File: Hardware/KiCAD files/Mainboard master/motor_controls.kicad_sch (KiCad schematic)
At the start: 78 parts, among them J11 Conn_01x08, J12 Conn_01x08, J2 Conn_01x06, J4 Conn_01x06, J5 PINHD_1x8_Male, J6 Conn_01x06, J7 Conn_01x06, J9 PINHD_1x8_Male, U10 DRV8825PWPR, U4 DRV8825PWPR, U5 DRV8825PWPR, U8 DRV8825PWPR, U9 DRV8825PWPR

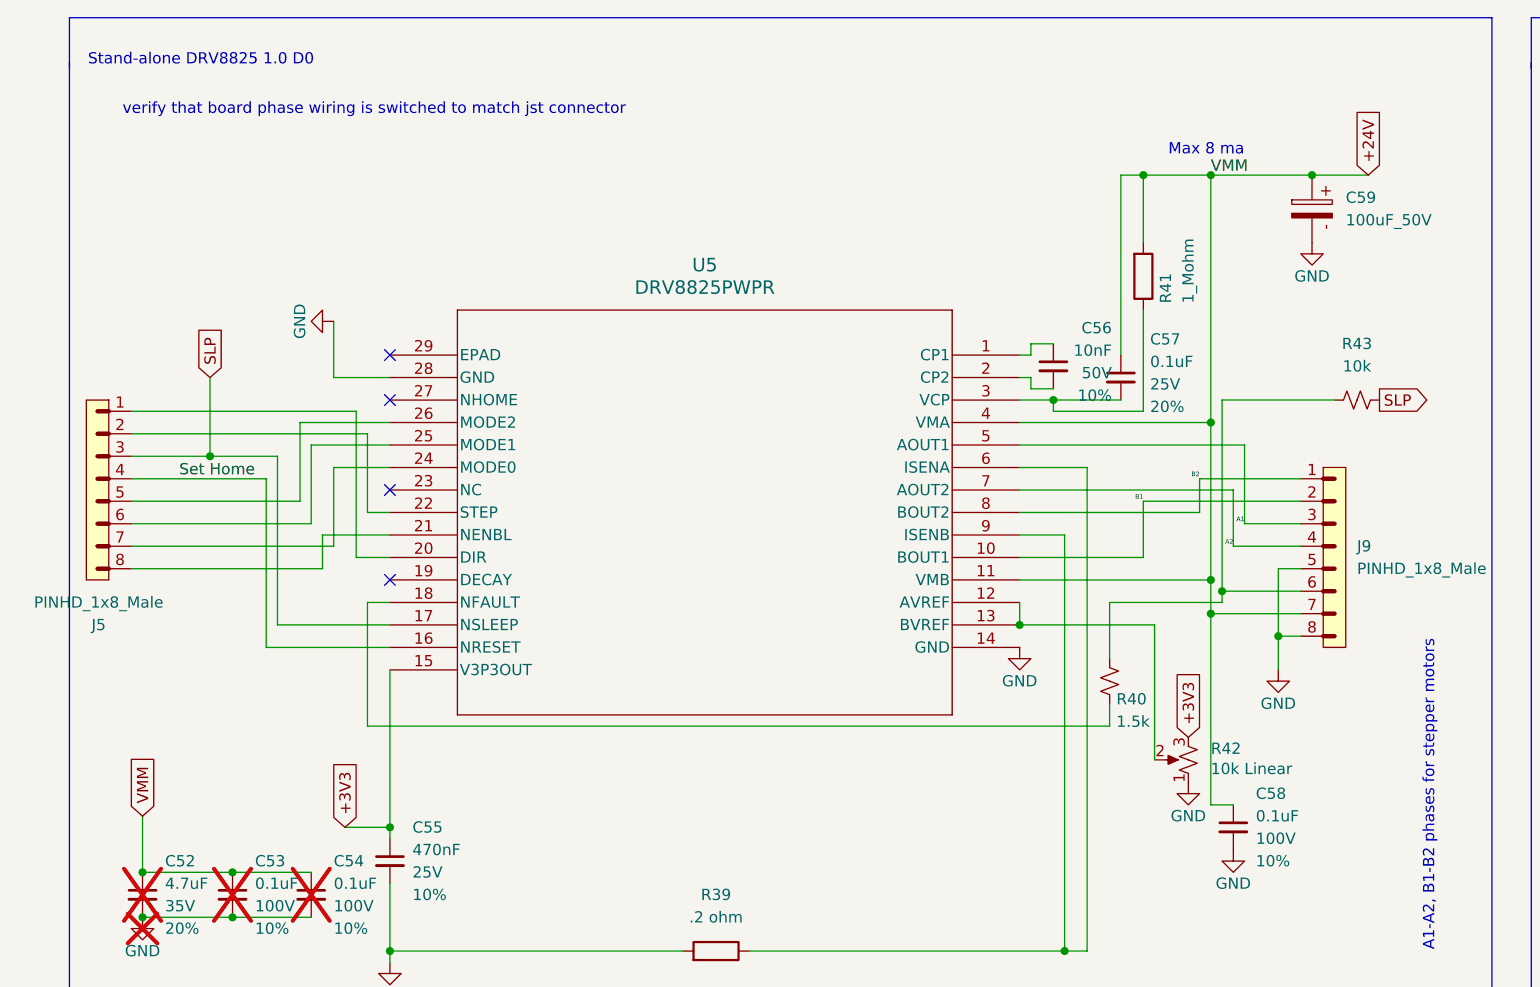
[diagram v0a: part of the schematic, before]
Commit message: 1st push of PCB's for printing
This is pre-peer review. This almost certainly has section that need adjustment. also realized I'm missing the USB-Uart bridge. first thing added in next version.
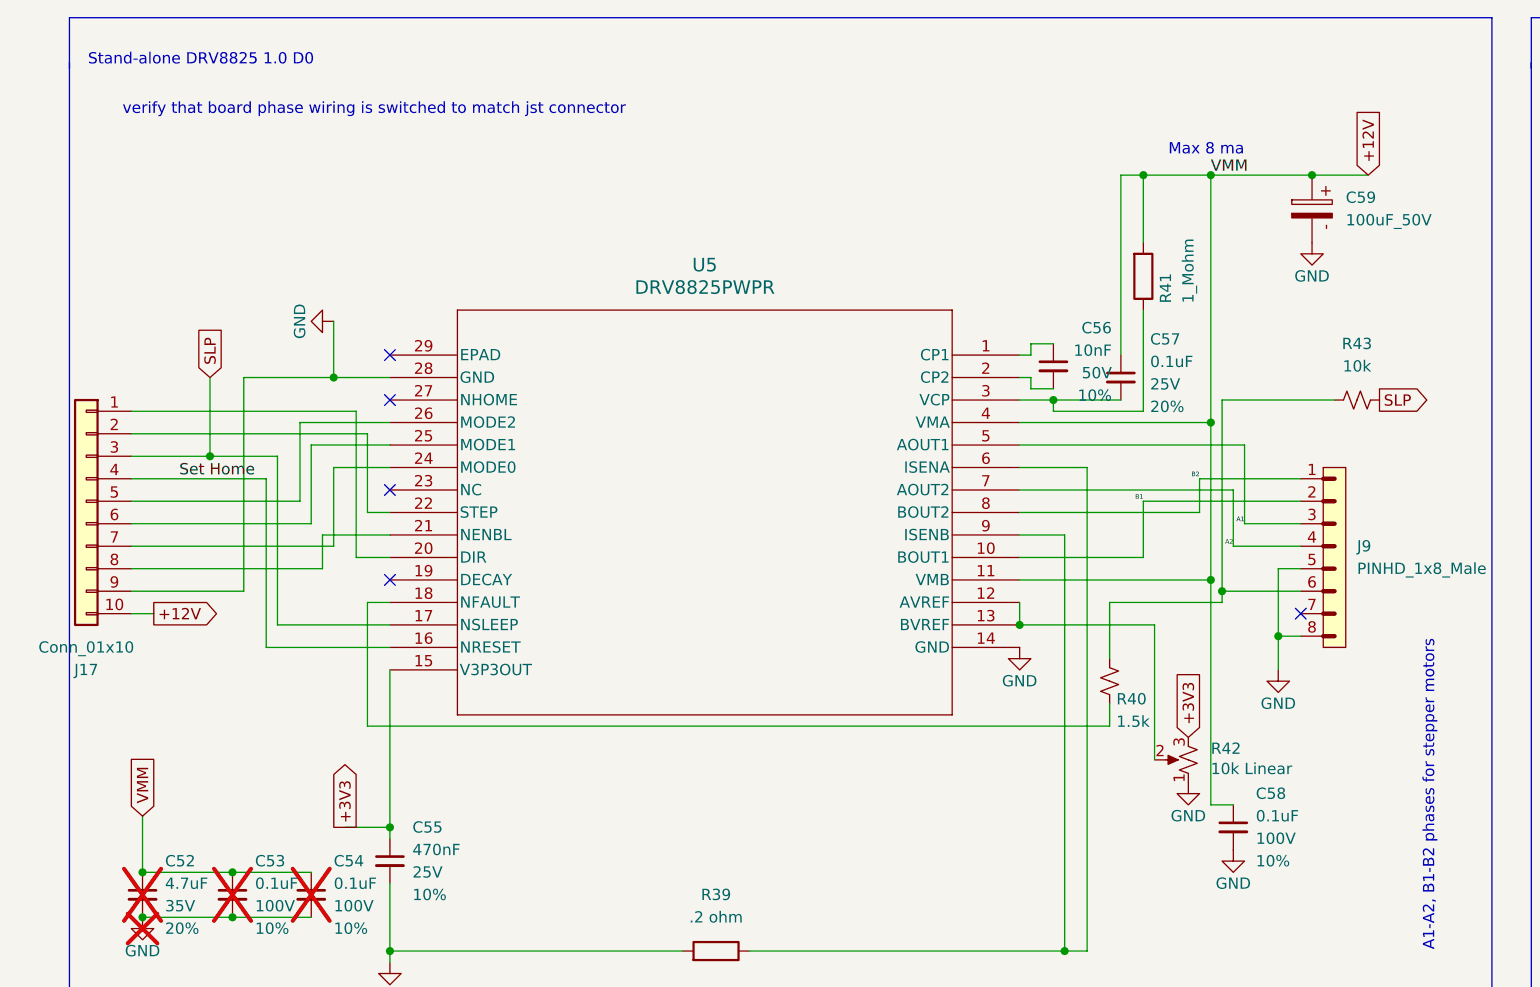
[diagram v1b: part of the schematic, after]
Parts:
- removed J5: PINHD_1x8_Male, Connector_PinHeader_2.54mm:PinHeader_1x08_P2.54mm_Vertical, symbol PCM_SL_Pin_Headers:PINHD_1x8_Male
- added J17: Conn_01x10, PCM_SparkFun-Connector:1x10_P2.54mm, symbol PCM_SparkFun-Connector:Conn_01x10_P2.54mm
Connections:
- net GND: now also J17.9 (Pin_9)
- net NRESET: now also J17.4 (Pin_4)
- net SLP: now also J17.3 (Pin_3)
- net at U5.20 (DIR): now also J17.1 (Pin_1)
- net at U5.21 (NENBL): now also J17.8 (Pin_8)
- net at U5.22 (STEP): now also J17.2 (Pin_2)
- net at U5.24 (MODE0): now also J17.7 (Pin_7)
- net at U5.25 (MODE1): now also J17.6 (Pin_6)
- net at U5.26 (MODE2): now also J17.5 (Pin_5)
- net +24V renamed +12V
- net +12V: now also J17.10 (Pin_10); no longer J9.7
- no-connect marks 28 -> 29
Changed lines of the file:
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@@
 	)
 	(junction
-		(at 146.05 81.28)
-		(diameter 0)
-		(color 0 0 0 0)
-	)
-	(junction
 		(at 123.19 85.09)
 		(diameter 0)
@@
 	)
 	(junction
+		(at 45.72 57.15)
+		(diameter 0)
+		(color 0 0 0 0)
+	)
+	(junction
 		(at 486.41 39.37)
 		(diameter 0)
@@
 	)
 	(junction
+		(at 146.05 81.28)
+		(diameter 0)
+		(color 0 0 0 0)
+	)
+	(junction
 		(at 199.39 113.03)
 		(diameter 0)
@@
 	)
 	(junction
-		(at 144.78 83.82)
-		(diameter 0)
-		(color 0 0 0 0)
-	)
-	(junction
 		(at 321.31 34.29)
 		(diameter 0)
@@
 		(at 50.8 222.25)
 	)
+	(no_connect
+		(at 154.94 83.82)
+	)
 	(wire
 		(pts
@@
 	(wire
 		(pts
-			(xy 217.17 72.39) (xy 214.63 72.39)
+			(xy 35.56 57.15) (xy 45.72 57.15)
 		)
 		(stroke
@@
 	(wire
 		(pts
-			(xy 534.67 318.77) (xy 543.56 318.77)
+			(xy 217.17 72.39) (xy 214.63 72.39)
 		)
 		(stroke
@@
 	(wire
 		(pts
-			(xy 22.86 60.96) (xy 48.26 60.96)
+			(xy 534.67 318.77) (xy 543.56 318.77)
 		)
 		(stroke
@@
 	(wire
 		(pts
-			(xy 478.79 69.85) (xy 478.79 83.82)
+			(xy 22.86 60.96) (xy 48.26 60.96)
 		)
 		(stroke
@@
 	(wire
 		(pts
-			(xy 52.07 87.63) (xy 38.1 87.63)
+			(xy 478.79 69.85) (xy 478.79 83.82)
 		)
 		(stroke
@@
 	(wire
 		(pts
-			(xy 303.53 85.09) (xy 303.53 100.33)
+			(xy 52.07 87.63) (xy 38.1 87.63)
 		)
 		(stroke
@@
 	(wire
 		(pts
-			(xy 288.29 77.47) (xy 302.26 77.47)
+			(xy 303.53 85.09) (xy 303.53 100.33)
 		)
 		(stroke
@@
 	(wire
 		(pts
-			(xy 137.16 34.29) (xy 137.16 41.91)
+			(xy 288.29 77.47) (xy 302.26 77.47)
 		)
 		(stroke
@@
 	(wire
 		(pts
-			(xy 146.05 81.28) (xy 154.94 81.28)
+			(xy 137.16 34.29) (xy 137.16 41.91)
 		)
 		(stroke
@@
 	(wire
 		(pts
+			(xy 146.05 81.28) (xy 146.05 82.55)
+		)
+		(stroke
+			(width 0)
+			(type default)
+		)
+	)
+	(wire
+		(pts
 			(xy 382.27 119.38) (xy 382.27 127)
 		)
@@
 	(wire
 		(pts
+			(xy 35.56 81.28) (xy 35.56 57.15)
+		)
+		(stroke
+			(width 0)
+			(type default)
+		)
+	)
+	(wire
+		(pts
 			(xy 457.2 64.77) (xy 457.2 66.04)
 		)
@@
 	(wire
 		(pts
+			(xy 146.05 81.28) (xy 154.94 81.28)
+		)
+		(stroke
+			(width 0)
+			(type default)
+		)
+	)
+	(wire
+		(pts
 			(xy 152.4 86.36) (xy 152.4 78.74)
 		)
@@
 	(wire
 		(pts
-			(xy 144.78 80.01) (xy 144.78 83.82)
+			(xy 144.78 80.01) (xy 144.78 105.41)
 		)
 		(stroke
@@
 	(wire
 		(pts
-			(xy 144.78 83.82) (xy 154.94 83.82)
-		)
-		(stroke
-			(width 0)
-			(type default)
-		)
-	)
-	(wire
-		(pts
 			(xy 210.82 208.28) (xy 210.82 217.17)
 		)
@@
 		)
 	)
-	(wire
-		(pts
-			(xy 146.05 59.69) (xy 146.05 81.28)
-		)
-		(stroke
-			(width 0)
-			(type default)
-		)
-	)
 	(polyline
 		(pts
@@
 	(wire
 		(pts
+			(xy 22.86 81.28) (xy 35.56 81.28)
+		)
+		(stroke
+			(width 0)
+			(type default)
+		)
+	)
+	(wire
+		(pts
 			(xy 22.86 66.04) (xy 31.75 66.04)
 		)
@@
 	(wire
 		(pts
-			(xy 146.05 81.28) (xy 146.05 82.55)
+			(xy 146.05 59.69) (xy 146.05 81.28)
 		)
 		(stroke
@@
 	(wire
 		(pts
-			(xy 144.78 83.82) (xy 144.78 105.41)
-		)
-		(stroke
-			(width 0)
-			(type default)
-		)
-	)
-	(wire
-		(pts
 			(xy 292.1 200.66) (xy 292.1 201.93)
 		)
@@
 	(wire
 		(pts
+			(xy 25.4 83.82) (xy 22.86 83.82)
+		)
+		(stroke
+			(width 0)
+			(type default)
+		)
+	)
+	(wire
+		(pts
 			(xy 453.39 72.39) (xy 461.01 72.39)
 		)
@@
 	)
 	(global_label "+3V3"
-		(shape input)
+		(shape output)
 		(at 46.99 107.95 90)
 		(fields_autoplaced yes)
@@
 		)
 	)
-	(global_label "+24V"
+	(global_label "+12V"
 		(shape input)
 		(at 162.56 34.29 90)
@@
 		)
 	)
+	(global_label "+12V"
+		(shape output)
+		(at 25.4 83.82 0)
+		(fields_autoplaced yes)
+		(effects
+			(font
+				(size 1.27 1.27)
+			)
+			(justify left)
+		)
+		(property "Intersheetrefs" "${INTERSHEET_REFS}"
+			(at 33.4652 83.82 0)
+			(hide yes)
+			(show_name no)
+			(do_not_autoplace no)
+			(effects
+				(font
+					(size 1.27 1.27)
+				)
+				(justify left)
+			)
+		)
+	)
 	(global_label "N_FAULT"
 		(shape output)
@@
 	)
 	(symbol
-		(lib_id "PCM_SL_Pin_Headers:PINHD_1x8_Male")
-		(at 19.05 69.85 0)
-		(mirror y)
-		(unit 1)
-		(body_style 1)
-		(exclude_from_sim no)
-		(in_bom yes)
-		(on_board yes)
-		(in_pos_files yes)
-		(dnp no)
-		(property "Reference" "J5"
-			(at 19.175 85.09 0)
-			(show_name no)
-			(do_not_autoplace no)
-			(effects
-				(font
-					(size 1.27 1.27)
-				)
-			)
-		)
-		(property "Value" "PINHD_1x8_Male"
-			(at 19.175 82.55 0)
-			(show_name no)
-			(do_not_autoplace no)
-			(effects
-				(font
-					(size 1.27 1.27)
-				)
-			)
-		)
-		(property "Footprint" "Connector_PinHeader_2.54mm:PinHeader_1x08_P2.54mm_Vertical"
-			(at 20.32 53.34 0)
-			(hide yes)
-			(show_name no)
-			(do_not_autoplace no)
-			(effects
-				(font
-					(size 1.27 1.27)
-				)
-			)
-		)
-		(property "Datasheet" ""
-			(at 19.05 54.61 0)
-			(hide yes)
-			(show_name no)
-			(do_not_autoplace no)
-			(effects
-				(font
-					(size 1.27 1.27)
-				)
-			)
-		)
-		(property "Description" "Pin Header male with pin space 2.54mm. Pin Count -8"
-			(at 19.05 69.85 0)
-			(hide yes)
-			(show_name no)
-			(do_not_autoplace no)
-			(effects
-				(font
-					(size 1.27 1.27)
-				)
-			)
-		)
-		(pin "5"
-		)
-		(pin "2"
-		)
-		(pin "3"
-		)
-		(pin "8"
-		)
-		(pin "4"
-		)
-		(pin "1"
-		)
-		(pin "7"
-		)
-		(pin "6"
-		)
-		(instances
-			(project "Senior design Mainboard"
-				(path "/1027da72-a2dd-4309-b004-99ab5e04adbe/4b2fef9b-8f47-474a-ba15-59630a0bd0a3"
-					(reference "J5")
-					(unit 1)
-				)
-			)
-		)
-	)
-	(symbol
 		(lib_id "PCM_SparkFun-Capacitor:0.1uF_0603_100V_10%")
 		(at 199.39 115.57 0)
@@
 					(unit 1)
 				)
+			)
+		)
+	)
+	(symbol
+		(lib_id "PCM_SparkFun-Connector:Conn_01x10_P2.54mm")
+		(at 17.78 71.12 0)
+		(mirror y)
+		(unit 1)
+		(body_style 1)
+		(exclude_from_sim no)
+		(in_bom yes)
+		(on_board yes)
+		(in_pos_files yes)
+		(dnp no)
+		(property "Reference" "J17"
+			(at 17.78 90.17 0)
+			(show_name no)
+			(do_not_autoplace no)
+			(effects
+				(font
+					(size 1.27 1.27)
+				)
+			)
+		)
+		(property "Value" "Conn_01x10"
+			(at 17.78 87.63 0)
+			(show_name no)
+			(do_not_autoplace no)
+			(effects
+				(font
+					(size 1.27 1.27)
+				)
+			)
+		)
+		(property "Footprint" "PCM_SparkFun-Connector:1x10_P2.54mm"
+			(at 17.78 88.9 0)
+			(hide yes)
+			(show_name no)
+			(do_not_autoplace no)
+			(effects
+				(font
+					(size 1.27 1.27)
+				)
+			)
+		)
+		(property "Datasheet" ""
+			(at 17.78 91.44 0)
+			(hide yes)
+			(show_name no)
+			(do_not_autoplace no)
+			(effects
+				(font
+					(size 1.27 1.27)
+				)
+			)
+		)
+		(property "Description" "Basic 0.1\" PTH"
+			(at 17.78 93.98 0)
+			(hide yes)
+			(show_name no)
+			(do_not_autoplace no)
+			(effects
+				(font
+					(size 1.27 1.27)
+				)
+			)
+		)
+		(pin "5"
+		)
+		(pin "4"
+		)
+		(pin "3"
+		)
+		(pin "7"
+		)
+		(pin "2"
+		)
+		(pin "6"
+		)
+		(pin "8"
+		)
+		(pin "9"
+		)
+		(pin "10"
+		)
+		(pin "1"
+		)
+		(instances
+			(project "Senior design Mainboard"
+				(path "/1027da72-a2dd-4309-b004-99ab5e04adbe/4b2fef9b-8f47-474a-ba15-59630a0bd0a3"
+					(reference "J17")
+					(unit 1)
+				)

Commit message: general updates to the schematics and layouts
includes some backchecks tot he master schematic to be accurate for the paper
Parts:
- removed C10, C11, C13, C14, C15, C31, C32, C36, C39, C40, C44, C53, C54, C58, C9: 0.1uF, PCM_SparkFun-Capacitor:C_0603_1608Metric, symbol PCM_SparkFun-Capacitor:0.1uF_0603_100V_10%
- removed C12, C19, C37, C45, C59: 100uF_50V, Capacitor_THT:CP_Radial_D8.0mm_P3.50mm, symbol PCM_SL_Capacitors:100uF_50V
- removed C17, C18, C30, C38, C52: 4.7uF, PCM_SparkFun-Capacitor:C_0603_1608Metric, symbol PCM_SparkFun-Capacitor:4.7uF_0603_35V_20%
- removed C20, C27, C33, C41, C55: 470nF, PCM_SparkFun-Capacitor:C_0402_1005Metric, symbol PCM_SparkFun-Capacitor:470nF_0402_25V_10%
- removed C21, C28, C34, C42, C56: 10nF, PCM_SparkFun-Capacitor:C_0603_1608Metric, symbol PCM_SparkFun-Capacitor:10nF_0603_50V_10%
- removed C22, C29, C35, C43, C57: 0.1uF, PCM_SparkFun-Capacitor:C_0603_1608Metric, symbol PCM_SparkFun-Capacitor:0.1uF_0603_25V_20%
- removed J17: Conn_01x10, PCM_SparkFun-Connector:1x10_P2.54mm, symbol PCM_SparkFun-Connector:Conn_01x10_P2.54mm
- removed J2, J4, J6, J7: Conn_01x06, PCM_SparkFun-Connector:1x06_P2.54mm, symbol PCM_SparkFun-Connector:Conn_01x06_P2.54mm
- removed J9: PINHD_1x8_Male, Connector_PinHeader_2.54mm:PinHeader_1x08_P2.54mm_Vertical, symbol PCM_SL_Pin_Headers:PINHD_1x8_Male
- removed R10, R19, R24, R29, R40: 1.5k, PCM_SparkFun-Resistor:R_0603_1608Metric, symbol PCM_SparkFun-Resistor:1.5k_0603
- removed R11, R21, R26, R31, R42: 10k Linear, PCM_SparkFun-Resistor:Bourns-PDB18, symbol PCM_SparkFun-Resistor:Trimpot_10k_RA_PTH
- removed R12, R22, R27, R32, R43: 10k, PCM_SparkFun-Resistor:R_0603_1608Metric, symbol PCM_SparkFun-Resistor:10k_0603
- removed R16, R20, R25, R30, R41: 1_Mohm, symbol PCM_Resistor_AKL:R_Generic
- removed R23, R28, R39, R4, R9: .2 ohm, symbol PCM_Resistor_AKL:R_Generic
- removed U10, U4, U5, U8, U9: DRV8825PWPR, symbol DRV8825PRPR driver chip:DRV8825PWPR
- added C1, C11, C13, C9: 470nF, PCM_SparkFun-Capacitor:C_0805_2012Metric, symbol PCM_SparkFun-Capacitor:470nF_0805_100V_10%
- added C10, C12, C14, C2: 100uF, PCM_SparkFun-Capacitor:C_1206_3216Metric, symbol PCM_SparkFun-Capacitor:100uF_1206_50V_10%
- added C68, C72, C76, C80: 10nF, PCM_SparkFun-Capacitor:C_0603_1608Metric, symbol PCM_SparkFun-Capacitor:10nF_0603_50V_10%
- added C69, C70, C73, C74, C77, C78, C81, C82: 0.1uF, PCM_SparkFun-Capacitor:C_0603_1608Metric, symbol PCM_SparkFun-Capacitor:0.1uF_0603_25V_20%
- added C71, C75, C79, C83: 0.1uF, PCM_SparkFun-Capacitor:C_0603_1608Metric, symbol PCM_SparkFun-Capacitor:0.1uF_0603_100V_10%
- added D16, D17, D18, D19: Blue, PCM_SparkFun-LED:LED_0603_1608Metric_Blue, symbol PCM_SparkFun-LED:LED_Blue_0603
- added J25, J26, J27, J30, J40, J41, J42, J43: PINHD_1x8_Male, Connector_PinHeader_2.54mm:PinHeader_1x08_P2.54mm_Vertical, symbol PCM_SL_Pin_Headers:PINHD_1x8_Male
- added JP1, JP2, JP3, JP4: (no value), PCM_SparkFun-Jumper:Jumper_2_NO, symbol PCM_SparkFun-Jumper:SolderJumper_2_Open
- added R10, R11, R12, R16, R19, R5, R6, R9: R_0805, PCM_Resistor_SMD_AKL:R_0805_2012Metric, symbol PCM_Resistor_AKL:R_0805
- added R49, R54, R73, R78: 1.5k, PCM_SparkFun-Resistor:R_0603_1608Metric, symbol PCM_SparkFun-Resistor:1.5k_0603
- added R50, R55, R74, R79: 2.2k, PCM_SparkFun-Resistor:R_0603_1608Metric, symbol PCM_SparkFun-Resistor:2.2k_0603
- added R51, R70, R75, R80: 1 Mohm, Resistor_SMD:R_0603_1608Metric, symbol PCM_SL_Resistors:Resistor
- added R52, R53, R71, R72, R76, R77, R81, R82: 10k, PCM_SparkFun-Resistor:R_0603_1608Metric, symbol PCM_SparkFun-Resistor:10k_0603
- added U11, U12, U18, U19: DRV8825PWPR, DRV8825pwp:IC_TPS61196PWPRQ1, symbol DRV8825PRPR driver chip:DRV8825PWPR
- added VR1, VR2, VR3, VR4: 3361P-1-104GLF, 100k_trimmer_pot.:TRIM_3361P-1-104GLF, symbol 3361P-1-104GLF:3361P-1-104GLF
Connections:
- net +12V: now also C10.1, C12.1, C14.1, C2.1, C69.2, C70.1, C71.1, C73.2, C74.1, C75.1, C77.2, C78.1, C79.1, C81.2, C82.1, C83.1, J26.1, J30.1, J41.1, J43.1, JP1.1 (A), JP2.1 (A), JP3.1 (A), JP4.1 (A), R51.1, R70.1, R75.1, R80.1, U11.11 (VMB), U11.4 (VMA), U12.11 (VMB), U12.4 (VMA), U18.11 (VMB), U18.4 (VMA), U19.11 (VMB), U19.4 (VMA)
- net +3V3: now also C1.1, C11.1, C13.1, C9.1, U11.15 (V3P3OUT), U12.15 (V3P3OUT), U18.15 (V3P3OUT), U19.15 (V3P3OUT), VR1.3, VR2.3, VR3.3, VR4.3
- net A1: now also J26.5, J30.5, J41.5, J43.5, U11.5 (AOUT1), U12.5 (AOUT1), U18.5 (AOUT1), U19.5 (AOUT1)
- net A2: now also J26.6, J30.6, J41.6, J43.6, U11.7 (AOUT2), U12.7 (AOUT2), U18.7 (AOUT2), U19.7 (AOUT2)
- net B1: now also J26.4, J30.4, J41.4, J43.4, U11.10 (BOUT1), U12.10 (BOUT1), U18.10 (BOUT1), U19.10 (BOUT1)
- net B2: now also J26.3, J30.3, J41.3, J43.3, U11.8 (BOUT2), U12.8 (BOUT2), U18.8 (BOUT2), U19.8 (BOUT2)
- net GND: now also C1.2, C10.2, C11.2, C12.2, C13.2, C14.2, C2.2, C70.2, C71.2, C74.2, C75.2, C78.2, C79.2, C82.2, C83.2, C9.2, D16.1 (K), D17.1 (K), D18.1 (K), D19.1 (K), J26.2, J26.8, J30.2, J30.8, J41.2, J41.8, J43.2, J43.8, R10.2, R11.2, R12.2, R16.2, R19.2, R5.2, R6.2, R9.2, U11.14 (GND), U11.28 (GND), U11.29 (EPAD), U12.14 (GND), U12.28 (GND), U12.29 (EPAD), U18.14 (GND), U18.28 (GND), U18.29 (EPAD), U19.14 (GND), U19.28 (GND), U19.29 (EPAD), VR1.1, VR2.1, VR3.1, VR4.1
- net SLP: now also J25.3, J27.3, J40.3, J42.3, R53.2, R72.2, R77.2, R82.2, U11.17 (NSLEEP), U12.17 (NSLEEP), U18.17 (NSLEEP), U19.17 (NSLEEP)
- new net: C72.1, U12.1 (CP1)
- new net: C72.2, U12.2 (CP2)
- new net: C76.1, U18.1 (CP1)
- new net: C76.2, U18.2 (CP2)
- new net: C69.1, R51.2, U11.3 (VCP)
- new net: R73.1, U18.18 (NFAULT)
- new net: J41.7, R73.2, R76.1, R77.1
- new net: R6.1, U11.6 (ISENA)
- new net: J43.7, R78.2, R81.1, R82.1
- new net: C77.1, R75.2, U18.3 (VCP)
- new net: J30.7, R54.2, R71.1, R72.1
- new net: D17.2 (A), R55.2
- new net: C73.1, R70.2, U12.3 (VCP)
- new net: C68.1, U11.1 (CP1)
- new net: U11.12 (AVREF), U11.13 (BVREF), VR1.2
- new net: R49.1, U11.18 (NFAULT)
- new net: C68.2, U11.2 (CP2)
- new net: J25.1, U11.20 (DIR)
- new net: J25.8, U11.21 (NENBL)
- new net: J25.2, U11.22 (STEP)
- new net: J25.7, U11.24 (MODE0)
- new net: J25.6, U11.25 (MODE1)
- new net: J25.5, U11.26 (MODE2)
- new net: R5.1, U11.9 (ISENB)
- new net: R9.1, U12.9 (ISENB)
- new net: JP2.2 (B), R55.1
- new net: JP1.2 (B), R50.1
- new net: R16.1, U19.9 (ISENB)
- new net: J26.7, R49.2, R52.1, R53.1
- new net: C81.1, R80.2, U19.3 (VCP)
- new net: C80.1, U19.1 (CP1)
- new net: C80.2, U19.2 (CP2)
- new net: R12.1, U18.6 (ISENA)
- new net: JP3.2 (B), R74.1
- new net: D18.2 (A), R74.2
- new net: J27.1, U12.20 (DIR)
- new net: J27.2, U12.22 (STEP)
- new net: J27.5, U12.26 (MODE2)
- new net: J27.6, U12.25 (MODE1)
- new net: J27.7, U12.24 (MODE0)
- new net: J27.8, U12.21 (NENBL)
- new net: R54.1, U12.18 (NFAULT)
- new net: JP4.2 (B), R79.1
- new net: R19.1, U19.6 (ISENA)
- new net: R10.1, U12.6 (ISENA)
- new net: U18.12 (AVREF), U18.13 (BVREF), VR3.2
- new net: J40.1, U18.20 (DIR)
- new net: J40.8, U18.21 (NENBL)
- new net: J40.2, U18.22 (STEP)
- new net: J40.7, U18.24 (MODE0)
- new net: J40.6, U18.25 (MODE1)
- new net: J40.5, U18.26 (MODE2)
- new net: R11.1, U18.9 (ISENB)
- new net: U12.12 (AVREF), U12.13 (BVREF), VR2.2
- new net: J42.1, U19.20 (DIR)
- new net: J42.2, U19.22 (STEP)
- new net: J42.5, U19.26 (MODE2)
- new net: J42.6, U19.25 (MODE1)
- new net: J42.7, U19.24 (MODE0)
- new net: J42.8, U19.21 (NENBL)
- new net: U19.12 (AVREF), U19.13 (BVREF), VR4.2
- new net: R78.1, U19.18 (NFAULT)
- new net: D19.2 (A), R79.2
- new net: D16.2 (A), R50.2
- new net RESET: J25.4, J27.4, J40.4, J42.4, R52.2, R71.2, R76.2, R81.2, U11.16 (NRESET), U12.16 (NRESET), U18.16 (NRESET), U19.16 (NRESET)
- no-connect marks 29 -> 12
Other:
- note added: "Stand-alone DRV8825 1.2 D0"
- note removed: "DRV8825 1.1 D0"
- note removed: "DRV8825 1.1 D02"
- note removed: "DRV8825 1.1 D03 Extruder"
- note removed: "DRV8825 1.1 D1"
- note removed: "NoteMeausure impedance of the lines in layout ISA and ISB are .20 ohm, do with wire parasitics"
- note removed: "Replace all generics for specific componenets"
- note removed: "Stand-alone DRV8825 1.0 D0"
